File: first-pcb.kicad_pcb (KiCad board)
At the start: 2 copper layers, 88.9 x 45.7 mm, 8 parts, among them K1 my_connector, P1 10k, Q1 BC547, U1 LM358

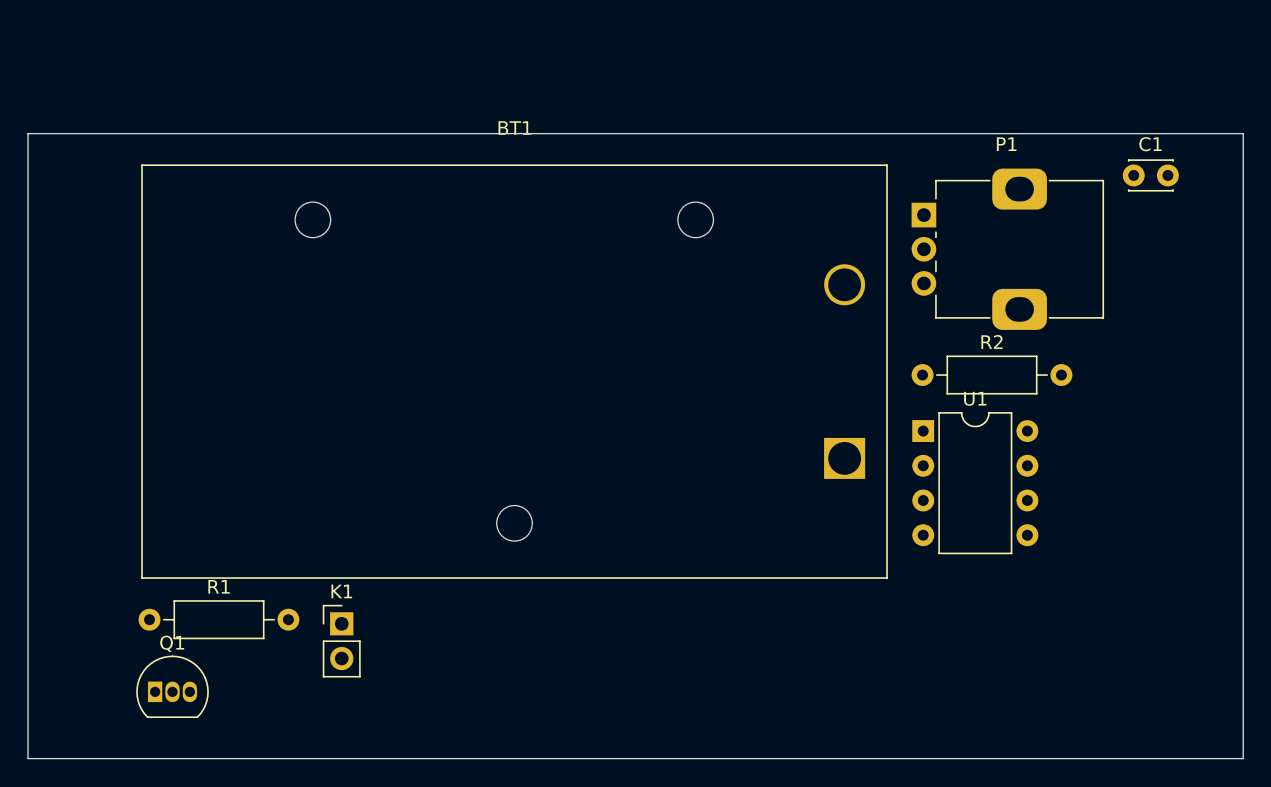
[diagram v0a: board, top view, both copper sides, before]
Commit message: Component Place
Components from imported netlist are now organized better.
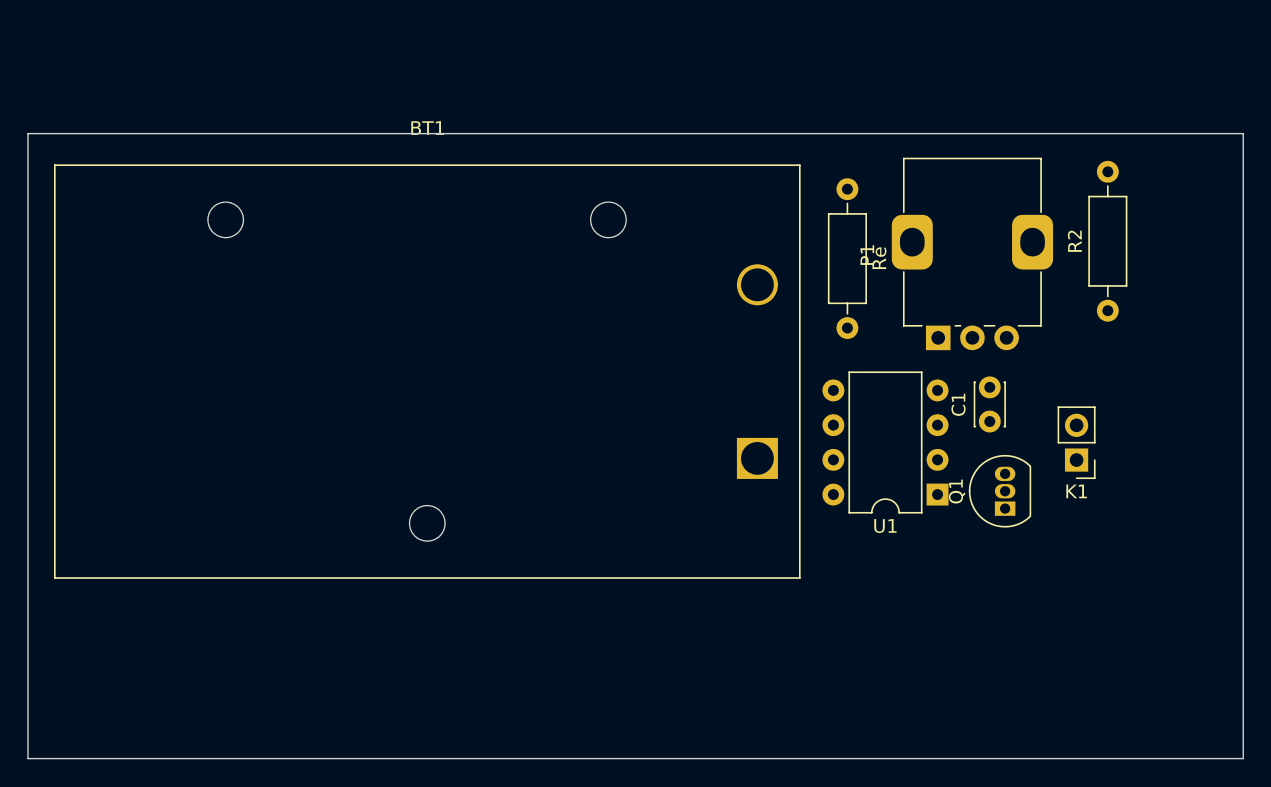
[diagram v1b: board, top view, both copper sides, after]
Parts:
- moved Q1 63.6 mm to (154.0, 106.2), turned to 90 degrees
- moved Re 60.0 mm to (142.5, 82.8), turned to -90 degrees
- moved K1 55.1 mm to (159.3, 102.6), turned to 180 degrees
- moved C1 20.9 mm to (152.9, 99.8), turned to 90 degrees
- moved R2 14.3 mm to (161.5, 91.7), turned to 90 degrees
- moved P1 9.04 mm to (149.1, 93.7), turned to 90 degrees
- moved BT1 6.38 mm to (135.9, 102.5)
- moved U1 4.76 mm to (149.1, 105.1), turned to 180 degrees
- renumbered R1 to Re

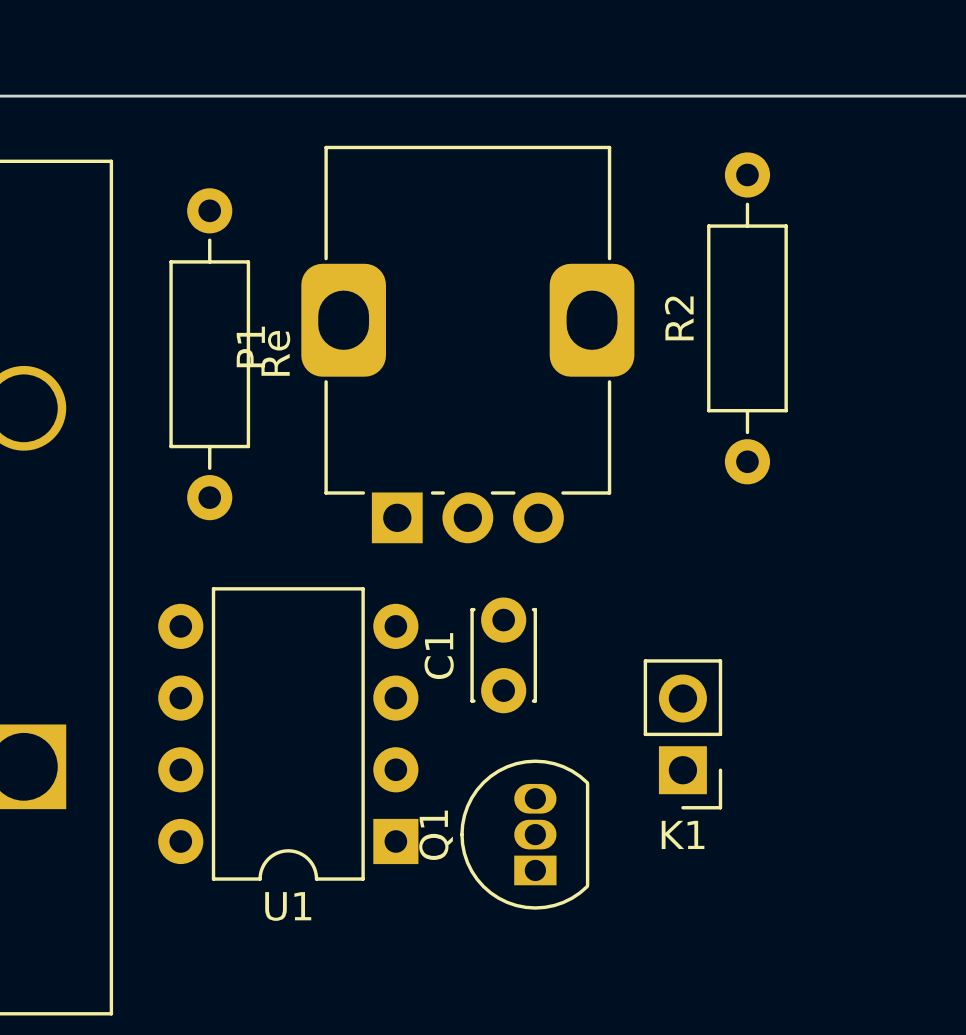
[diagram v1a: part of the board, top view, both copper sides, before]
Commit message: Connector Footprint Update
Added ground plane pins and resized the connector.
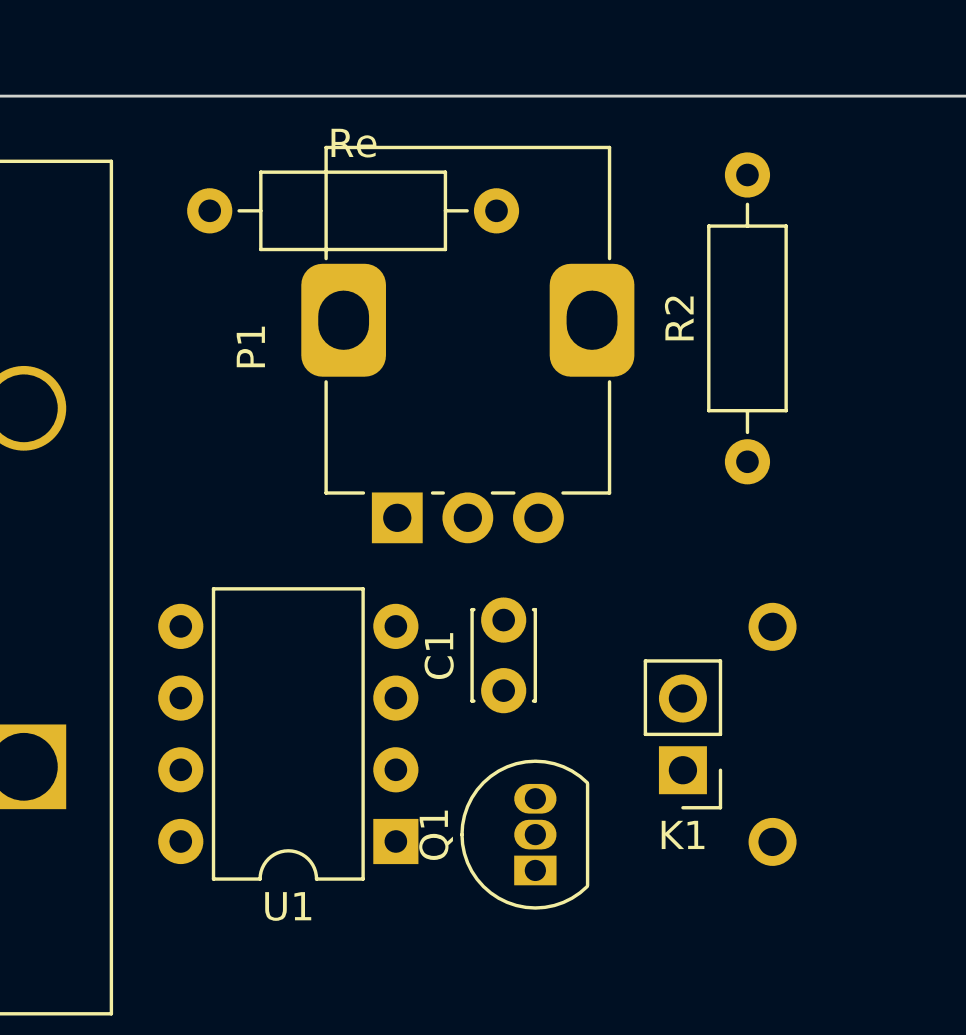
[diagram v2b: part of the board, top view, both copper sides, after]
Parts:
- turned Re to 0 degrees
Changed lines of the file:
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@@
   )
   (footprint "Resistor_THT:R_Axial_DIN0207_L6.3mm_D2.5mm_P10.16mm_Horizontal" (layer "F.Cu")
-    (at 142.494 82.804 -90)
+    (at 142.494 82.804)
     (descr "Resistor, Axial_DIN0207 series, Axial, Horizontal, pin pitch=10.16mm, 0.25W = 1/4W, length*diameter=6.3*2.5mm^2, http://cdn-reichelt.de/documents/datenblatt/B400/1_4W%23YAG.pdf")
     (tags "Resistor Axial_DIN0207 series Axial Horizontal pin pitch 10.16mm 0.25W = 1/4W length 6.3mm diameter 2.5mm")
@@
     (property "Sheetname" "")
     (attr through_hole)
-    (fp_text reference "Re" (at 5.08 -2.37 90) (layer "F.SilkS")
+    (fp_text reference "Re" (at 5.08 -2.37) (layer "F.SilkS")
       (effects (font (size 1 1) (thickness 0.15)))
     )
-    (fp_text value "100R" (at 5.08 2.37 90) (layer "F.Fab")
+    (fp_text value "100R" (at 5.08 2.37) (layer "F.Fab")
       (effects (font (size 1 1) (thickness 0.15)))
     )
-    (fp_text user "${REFERENCE}" (at 5.08 0 90) (layer "F.Fab")
+    (fp_text user "${REFERENCE}" (at 5.08 0) (layer "F.Fab")
       (effects (font (size 1 1) (thickness 0.15)))
     )
@@
     (fp_line (start 8.23 1.25) (end 8.23 -1.25) (layer "F.Fab") (width 0.1))
     (fp_line (start 1.93 1.25) (end 8.23 1.25) (layer "F.Fab") (width 0.1))
-    (pad "1" thru_hole circle (at 0 0 270) (size 1.6 1.6) (drill 0.8) (layers *.Cu *.Mask)
+    (pad "1" thru_hole circle (at 0 0) (size 1.6 1.6) (drill 0.8) (layers *.Cu *.Mask)
       (net 1 "Net-(BT1-Pad1)") (pintype "passive"))
-    (pad "2" thru_hole oval (at 10.16 0 270) (size 1.6 1.6) (drill 0.8) (layers *.Cu *.Mask)
+    (pad "2" thru_hole oval (at 10.16 0) (size 1.6 1.6) (drill 0.8) (layers *.Cu *.Mask)
       (net 2 "Net-(P1-Pad1)") (pintype "passive"))
     (model "${KICAD6_3DMODEL_DIR}/Resistor_THT.3dshapes/R_Axial_DIN0207_L6.3mm_D2.5mm_P10.16mm_Horizontal.wrl"
@@
     (fp_line (start -1.33 1.27) (end -1.33 3.87) (layer "F.SilkS") (width 0.12))
     (fp_line (start -1.33 -1.33) (end 0 -1.33) (layer "F.SilkS") (width 0.12))
-    (fp_line (start -1.8 4.35) (end 1.8 4.35) (layer "F.CrtYd") (width 0.05))
-    (fp_line (start 1.8 4.35) (end 1.8 -1.8) (layer "F.CrtYd") (width 0.05))
-    (fp_line (start -1.8 -1.8) (end -1.8 4.35) (layer "F.CrtYd") (width 0.05))
-    (fp_line (start 1.8 -1.8) (end -1.8 -1.8) (layer "F.CrtYd") (width 0.05))
+    (fp_line (start -4.4196 6.096) (end 1.8 6.096) (layer "F.CrtYd") (width 0.05))
+    (fp_line (start 1.8 6.096) (end 1.8 -3.556) (layer "F.CrtYd") (width 0.05))
+    (fp_line (start -4.4196 -3.556) (end -4.4196 6.096) (layer "F.CrtYd") (width 0.05))
+    (fp_line (start 1.8 -3.556) (end -4.4196 -3.556) (layer "F.CrtYd") (width 0.05))
     (fp_line (start -1.27 3.81) (end -1.27 -0.635) (layer "F.Fab") (width 0.1))
     (fp_line (start 1.27 3.81) (end -1.27 3.81) (layer "F.Fab") (width 0.1))
@@
     (pad "1" thru_hole rect (at 0 0 180) (size 1.7 1.7) (drill 1) (layers *.Cu *.Mask)
       (net 7 "Net-(K1-Pad1)") (pintype "input"))
-    (pad "2" thru_hole oval (at 0 2.54 180) (size 1.7 1.7) (drill 1) (layers *.Cu *.Mask)
+    (pad "2" thru_hole circle (at 0 2.54 180) (size 1.7 1.7) (drill 1) (layers *.Cu *.Mask)
       (net 4 "GND") (pintype "input"))
+    (pad "3" thru_hole circle (at -3.175 5.08 180) (size 1.7 1.7) (drill 1) (layers *.Cu *.Mask))
+    (pad "3" thru_hole circle (at -3.175 -2.54 180) (size 1.7 1.7) (drill 1) (layers *.Cu *.Mask))
     (model "${KICAD6_3DMODEL_DIR}/Connector_PinHeader_2.54mm.3dshapes/PinHeader_1x02_P2.54mm_Vertical.wrl"
       (offset (xyz 0 0 0))
